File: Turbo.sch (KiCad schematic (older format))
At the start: 16 parts, among them U12 74HCT27, U13 74HCT74, U14 74F86, U15 74F74, U16 74HCT04, U17 74HCT112, U18 74F157, U19 74F157

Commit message: finish routing
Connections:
- net 14M: now also U19.10 (I1c); no longer U19.6 (I1b)
- net 7M: now also U16.5, U19.11 (I0c); no longer U16.3, U19.5 (I0b)
- net CLK_CPU: now also U19.9 (Zc); no longer U19.7 (Zb)
- net GND: now also U16.3, U18.2 (I0a), U18.3 (I1a), U18.5 (I0b), U18.6 (I1b); no longer U16.9, U19.13 (I1d), U19.14 (I0d), U19.2 (I0a), U19.3 (I1a)
- net ~AS: now also U12.10, U16.9; no longer U12.2, U16.5
- net ~DTACK_BUS: now also U12.9, U19.5 (I0b); no longer U12.1, U19.10 (I1c)
- net ~DTACK_CPU: now also U19.7 (Zb); no longer U19.9 (Zc)
- net ~VMA_BUS: now also U19.4 (Za); no longer U18.4 (Za)
- net ~VMA_CPU: now also U19.2 (I0a); no longer U18.2 (I0a)
- net ~VPA_BUS: now also U19.14 (I0d); no longer U18.5 (I0b)
- net ~VPA_CPU: now also U19.12 (Zd); no longer U18.7 (Zb)
- net at U15.1 (~R), U15.10 (~S), U17.14 (~R): now also U16.8; no longer U16.6
- net at U15.2 (D): now also U12.8; no longer U12.12
- net at U15.11 (C), U15.3 (C): now also U16.6; no longer U16.4
- net at U15.6 (~Q): now also U19.6 (I1b); no longer U19.11 (I0c)
- net at U15.9 (Q): now also U12.11; no longer U12.13
- new net: U17.7 (~Q), U19.13 (I1d), U19.3 (I1a)
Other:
- moved on the sheet: U16B, U16C, U16D
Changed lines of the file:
@@
 Text HLabel 1050 2750 0    50   Input ~ 0
 ~AS
-Text HLabel 7800 1200 2    50   Output ~ 0
+Text HLabel 7800 3400 2    50   Output ~ 0
 ~VMA_BUS
-Text HLabel 7800 1500 2    50   Output ~ 0
+Text HLabel 7800 4300 2    50   Output ~ 0
 ~VPA_CPU
-Text HLabel 7800 4000 2    50   Output ~ 0
+Text HLabel 7800 3700 2    50   Output ~ 0
 ~DTACK_CPU
 Text HLabel 1150 3700 0    50   Input ~ 0
@@
 L 74:74HCT04 U16
 U 3 1 606DDE8E
+P 1650 4150
+F 0 "U16" H 1600 4150 50  0000 C CNN
+F 1 "74HCT04" H 1650 4376 50  0000 C CNN
+F 2 "Package_DIP:DIP-14_W7.62mm" H 1650 4150 50  0001 C CNN
+F 3 "https://assets.nexperia.com/documents/data-sheet/74HC_HCT04.pdf" H 1650 4150 50  0001 C CNN
+	3    1650 4150
+	1    0    0    -1
+$EndComp
+$Comp
+L 74:74HCT04 U16
+U 4 1 606DE635
 P 1650 3100
-F 0 "U16" H 1600 3100 50  0000 C CNN
+F 0 "U16" H 1650 3417 50  0000 C CNN
 F 1 "74HCT04" H 1650 3326 50  0000 C CNN
 F 2 "Package_DIP:DIP-14_W7.62mm" H 1650 3100 50  0001 C CNN
 F 3 "https://assets.nexperia.com/documents/data-sheet/74HC_HCT04.pdf" H 1650 3100 50  0001 C CNN
-	3    1650 3100
-	1    0    0    -1
-$EndComp
-$Comp
-L 74:74HCT04 U16
-U 4 1 606DE635
-P 5550 6800
-F 0 "U16" H 5550 7117 50  0000 C CNN
-F 1 "74HCT04" H 5550 7026 50  0000 C CNN
-F 2 "Package_DIP:DIP-14_W7.62mm" H 5550 6800 50  0001 C CNN
-F 3 "https://assets.nexperia.com/documents/data-sheet/74HC_HCT04.pdf" H 5550 6800 50  0001 C CNN
-	4    5550 6800
+	4    1650 3100
 	1    0    0    -1
 $EndComp
@@
 L 74:74HCT04 U16
 U 2 1 606DFD1C
-P 1650 4150
-F 0 "U16" H 1600 4150 50  0000 C CNN
-F 1 "74HCT04" H 1650 4376 50  0000 C CNN
-F 2 "Package_DIP:DIP-14_W7.62mm" H 1650 4150 50  0001 C CNN
-F 3 "https://assets.nexperia.com/documents/data-sheet/74HC_HCT04.pdf" H 1650 4150 50  0001 C CNN
-	2    1650 4150
+P 5550 6800
+F 0 "U16" H 5500 6800 50  0000 C CNN
+F 1 "74HCT04" H 5550 7026 50  0000 C CNN
+F 2 "Package_DIP:DIP-14_W7.62mm" H 5550 6800 50  0001 C CNN
+F 3 "https://assets.nexperia.com/documents/data-sheet/74HC_HCT04.pdf" H 5550 6800 50  0001 C CNN
+	2    5550 6800
 	1    0    0    -1
 $EndComp
 $Comp
 L 74:74LS27 U12
-U 1 1 606E87B7
+U 3 1 606E87B7
 P 3450 3200
 F 0 "U12" H 3450 3200 50  0000 C CNN
@@
 F 2 "Package_DIP:DIP-14_W7.62mm" H 3450 3200 50  0001 C CNN
 F 3 "http://www.ti.com/lit/gpn/sn74LS27" H 3450 3200 50  0001 C CNN
-	1    3450 3200
+	3    3450 3200
 	1    0    0    -1
 $EndComp
@@
 Text Label 2100 4700 0    50   ~ 0
 14M
-Text HLabel 7800 3700 2    50   Output ~ 0
+Text HLabel 7800 4000 2    50   Output ~ 0
 CLK_CPU
 Wire Wire Line
@@
 	2200 1900 6800 1900
 Wire Wire Line
-	4550 3500 6600 3500
-Wire Wire Line
-	4550 3800 6800 3800
-Wire Wire Line
-	4550 3800 4550 4700
-Connection ~ 6800 4700
-Wire Wire Line
-	6800 4300 6800 4400
-Connection ~ 6800 4400
+	4550 3500 5450 3500
 Wire Wire Line
 	6800 2100 6800 2200
 Connection ~ 6800 2500
 Connection ~ 6800 2200
-Wire Wire Line
-	6800 4400 6800 4700
 Wire Wire Line
 	6800 2200 6800 2500
@@
 Wire Wire Line
 	1250 4150 1250 4600
+Text HLabel 6800 4000 0    50   Input ~ 0
+7M
 Text HLabel 6800 3700 0    50   Input ~ 0
-7M
-Text HLabel 6800 4100 0    50   Input ~ 0
 ~DTACK_BUS
-Text HLabel 6800 1500 0    50   Input ~ 0
-~VPA_BUS
-Text HLabel 6800 1200 0    50   Input ~ 0
+Text HLabel 6800 3400 0    50   Input ~ 0
 ~VMA_CPU
 $Comp
@@
 Connection ~ 7300 3100
 Wire Wire Line
-	6350 1600 6350 1300
-Connection ~ 6350 1600
-Wire Wire Line
-	6350 1600 6800 1600
-Wire Wire Line
-	6350 1300 6800 1300
-Wire Wire Line
 	3400 1600 6350 1600
 Wire Wire Line
@@
 Connection ~ 7300 900
 Wire Wire Line
-	6050 1450 6050 2800
+	6050 1450 6050 1500
 Wire Wire Line
 	6050 2800 6800 2800
@@
 $EndComp
 Wire Wire Line
-	6800 4000 6600 4000
-Wire Wire Line
-	6600 4000 6600 3500
-Wire Wire Line
-	6050 3300 6050 3400
-Wire Wire Line
-	6050 3400 6800 3400
-Connection ~ 6050 3400
-Wire Wire Line
-	6050 3400 6050 5000
-Wire Wire Line
-	6800 3500 6800 3400
-Connection ~ 6800 3400
+	6800 4100 4550 4100
+Wire Wire Line
+	4550 4100 4550 4700
+Wire Wire Line
+	5450 3800 5450 3500
+Wire Wire Line
+	5450 3800 6800 3800
+Text HLabel 6800 4300 0    50   Input ~ 0
+~VPA_BUS
+Wire Wire Line
+	6050 3300 6050 5000
+Wire Wire Line
+	6050 1500 6350 1500
+Wire Wire Line
+	6350 1500 6350 1300
+Wire Wire Line
+	6350 1300 6700 1300
+Connection ~ 6050 1500
+Wire Wire Line
+	6050 1500 6050 2800
+Wire Wire Line
+	6800 1200 6700 1200
+Wire Wire Line
+	6700 1200 6700 1300
+Connection ~ 6700 1300
+Wire Wire Line
+	6700 1300 6800 1300
+Wire Wire Line
+	6350 3500 6800 3500
+Wire Wire Line
+	6350 1600 6350 3500
+Wire Wire Line
+	6350 3500 6350 4400
+Wire Wire Line
+	6350 4400 6800 4400
+Connection ~ 6350 3500
+Wire Wire Line
+	6700 1300 6700 1500
+Wire Wire Line
+	6700 1500 6800 1500
+Wire Wire Line
+	6700 1500 6700 1600
+Wire Wire Line
+	6700 1600 6800 1600
+Connection ~ 6700 1500
 $EndSCHEMATC

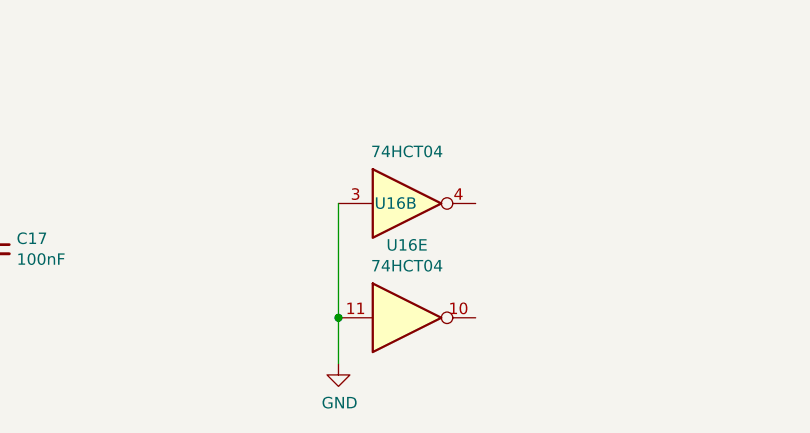
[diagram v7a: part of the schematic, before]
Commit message: dont mirror in lower 512k
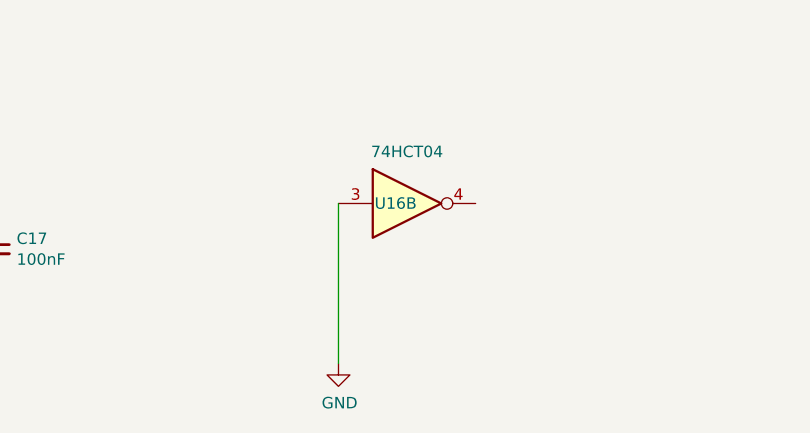
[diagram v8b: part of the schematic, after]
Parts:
- removed unit 5 of U16
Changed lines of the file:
@@
-$Comp
-L 74:74HCT04 U16
-U 5 1 606DF27D
-P 5550 7300
-F 0 "U16" H 5550 7617 50  0000 C CNN
-F 1 "74HCT04" H 5550 7526 50  0000 C CNN
-F 2 "Package_DIP:DIP-14_W7.62mm" H 5550 7300 50  0001 C CNN
-F 3 "https://assets.nexperia.com/documents/data-sheet/74HC_HCT04.pdf" H 5550 7300 50  0001 C CNN
-	5    5550 7300
-	1    0    0    -1
-$EndComp
 $Comp
 L 74:74HCT04 U16
@@
 	1    0    0    -1
 $EndComp
-Wire Wire Line
-	5250 7500 5250 7300
-Connection ~ 5250 7300
-Wire Wire Line
-	5250 7300 5250 6800
 $Comp
 L device:C_Small C18
@@
 	6700 1600 6800 1600
 Connection ~ 6700 1500
+Wire Wire Line
+	5250 6800 5250 7500
 $EndSCHEMATC
